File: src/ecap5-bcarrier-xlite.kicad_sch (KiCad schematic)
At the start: 27 parts, among them J3 VIN9_15, J4 GND, J5 USB_C_Receptacle_USB2.0_14P, SW1 RESET_SOM1, SW2 RESET_SOM2, SW3 USER1, SW4 USER2, U2 AP7375-33SA-7

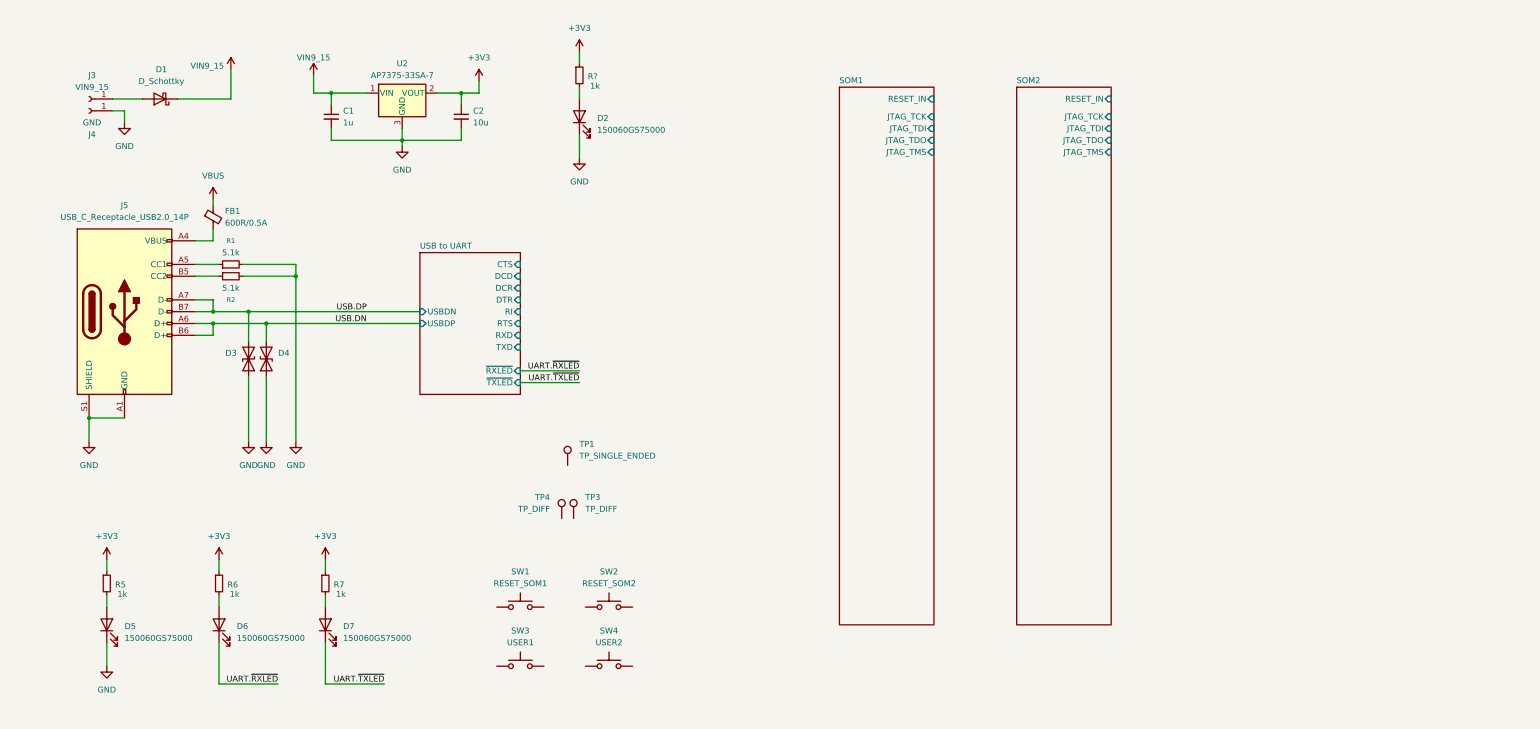
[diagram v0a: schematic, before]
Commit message: Add LED driver
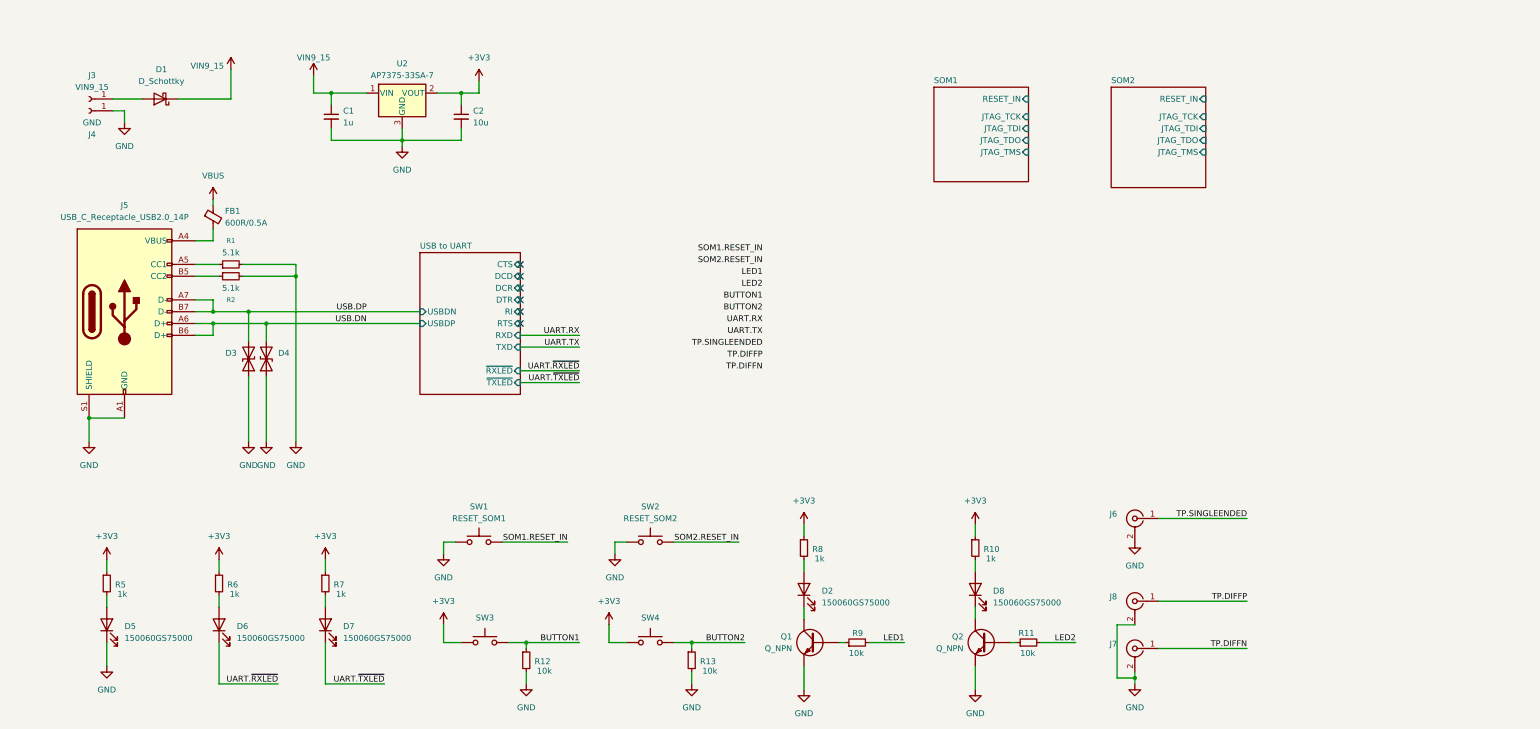
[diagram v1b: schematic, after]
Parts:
- removed R?: 1k, Resistor_SMD:R_0402_1005Metric, symbol Device:R_Small
- removed TP1: TP_SINGLE_ENDED, symbol Connector:TestPoint
- removed TP3, TP4: TP_DIFF, symbol Connector:TestPoint
- added D8: 150060GS75000, LED_SMD:LED_0603_1608Metric, symbol Device:LED
- added J6, J7, J8: Conn_Coaxial, symbol Connector:Conn_Coaxial
- added Q1, Q2: Q_NPN, symbol Device:Q_NPN
- added R10, R8: 1k, Resistor_SMD:R_0402_1005Metric, symbol Device:R_Small
- added R11, R12, R13, R9: 10k, Resistor_SMD:R_0402_1005Metric, symbol Device:R_Small
- SW4: value USER2 -> USER1
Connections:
- net +3V3: now also SW3.1, SW4.1, R10.1, R8.1
- net GND: now also SW1.1, SW2.1, J6.2 (Ext), J7.2 (Ext), J8.2 (Ext), Q1.E, Q2.E, R12.2, R13.2; no longer D2.1 (K)
- net SOM2.RESET_IN: now reaches SW2.2
- net SOM1.RESET_IN: now reaches SW1.2
- net at D2.2 (A): now also R8.2
- net BUTTON2: now reaches SW4.2
- net BUTTON2: now also R13.1
- net BUTTON1: now reaches SW3.2
- net BUTTON1: now also R12.1
- new net: Q2.B, R11.1
- new net: D8.1 (K), Q2.C
- new net: D2.1 (K), Q1.C
- new net: Q1.B, R9.1
- new net: D8.2 (A), R10.2
- new net LED1: R9.2
- new net LED2: R11.2
- new net TP.DIFFN: J7.1 (In)
- new net TP.DIFFP: J8.1 (In)
- new net TP.SINGLEENDED: J6.1 (In)
- no-connect marks 0 -> 6
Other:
- moved on the sheet: SW1, SW2, SW3

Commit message: Add component footprints
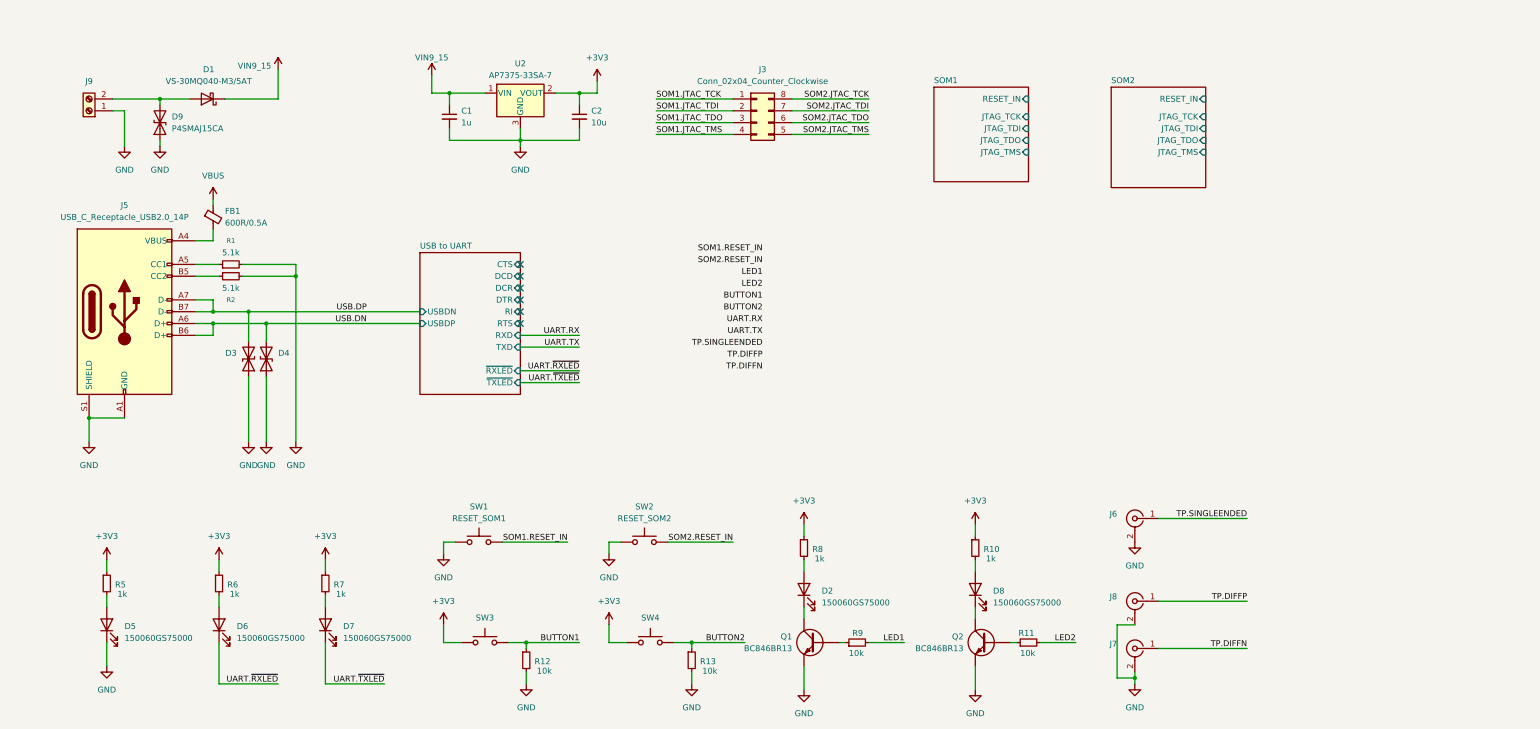
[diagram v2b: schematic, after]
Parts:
- removed J3: VIN9_15, symbol Connector:Conn_01x01_Socket
- removed J4: GND, symbol Connector:Conn_01x01_Socket
- added D9: P4SMAJ15CA, Diode_SMD:D_SMA, symbol Device:D_TVS
- added J3: Conn_02x04_Counter_Clockwise, Connector_PinSocket_2.54mm:PinSocket_2x04_P2.54mm_Vertical, symbol Connector_Generic:Conn_02x04_Counter_Clockwise
- added J9: 1935161, TerminalBlock_Phoenix:TerminalBlock_Phoenix_PT-1,5-2-5.0-H_1x02_P5.00mm_Horizontal, symbol Connector:Screw_Terminal_01x02
- C1, C2: footprint (none) -> Capacitor_SMD:C_0603_1608Metric
- D1: value D_Schottky -> VS-30MQ040-M3/5AT; footprint (none) -> Diode_SMD:D_SMA
- D3, D4: value D_TVS -> ESD321DYAR; footprint (none) -> Diode_SMD:D_SOD-523
- FB1: footprint (none) -> Inductor_SMD:L_0603_1608Metric; Part (none) -> MMZ1608Y601BTA00
- J5: footprint (none) -> Connector_USB:USB_C_Receptacle_GCT_USB4105-xx-A_16P_TopMnt_Horizontal; Part (none) -> USB4105-GF-A
- J6, J7, J8: footprint (none) -> Connector_Coaxial:SMA_Amphenol_132134-10_Vertical
- Q1, Q2: value Q_NPN -> BC846BR13; footprint (none) -> Package_TO_SOT_SMD:SOT-23-3
- R1, R2: footprint (none) -> Resistor_SMD:R_0603_1608Metric
- R10, R11, R12, R13, R5, R6, R7, R8, R9: footprint Resistor_SMD:R_0402_1005Metric -> Resistor_SMD:R_0603_1608Metric
- SW1, SW2, SW3, SW4: footprint (none) -> Button_Switch_SMD:SW_Push_1P1T_NO_CK_PTS125Sx73SMTR; Part (none) -> PTS125SM73SMTR21M LFS
- U2: footprint (none) -> Package_TO_SOT_SMD:SOT-23-3
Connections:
- net GND: now also D9.1 (A1), J9.1 (Pin_1)
- net at D1.2 (A): now also D9.2 (A2), J9.2 (Pin_2)
- new net SOM1.JTAC_TCK: J3.1 (Pin_1)
- new net SOM1.JTAC_TDI: J3.2 (Pin_2)
- new net SOM1.JTAC_TDO: J3.3 (Pin_3)
- new net SOM1.JTAC_TMS: J3.4 (Pin_4)
- new net SOM2.JTAC_TCK: J3.8 (Pin_8)
- new net SOM2.JTAC_TDI: J3.7 (Pin_7)
- new net SOM2.JTAC_TDO: J3.6 (Pin_6)
- new net SOM2.JTAC_TMS: J3.5 (Pin_5)
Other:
- moved on the sheet: C1, C2, D1, SW2, U2

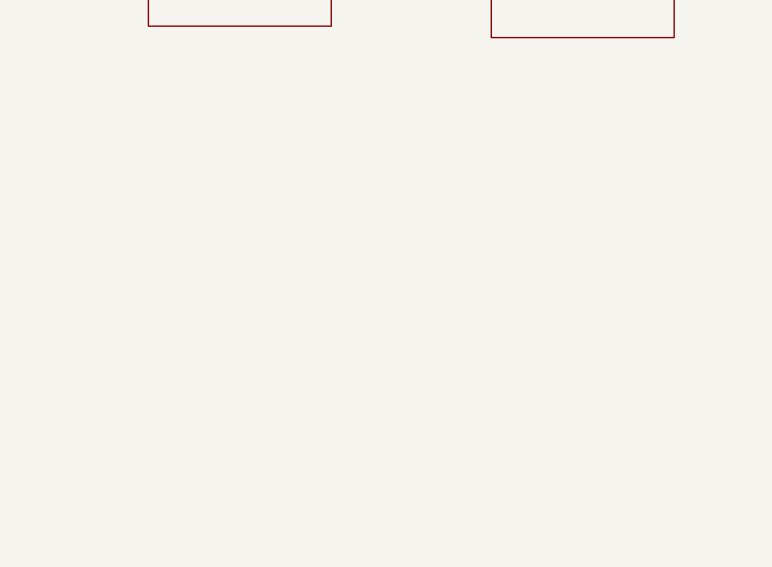
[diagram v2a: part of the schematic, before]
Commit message: Add power planes
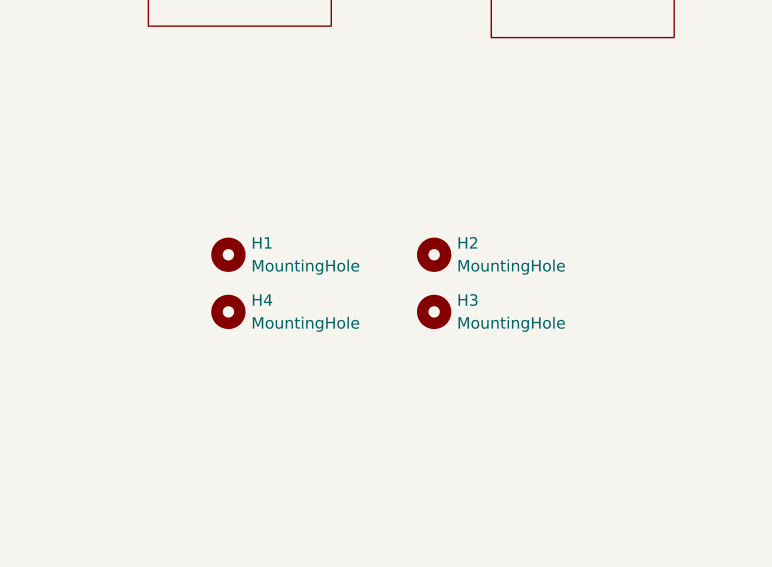
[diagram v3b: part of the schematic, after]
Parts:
- added H1, H2, H3, H4: MountingHole, MountingHole:MountingHole_2.2mm_M2, symbol Mechanical:MountingHole
- J3: footprint Connector_PinSocket_2.54mm:PinSocket_2x04_P2.54mm_Vertical -> Connector_PinHeader_2.54mm:PinHeader_2x04_P2.54mm_Vertical

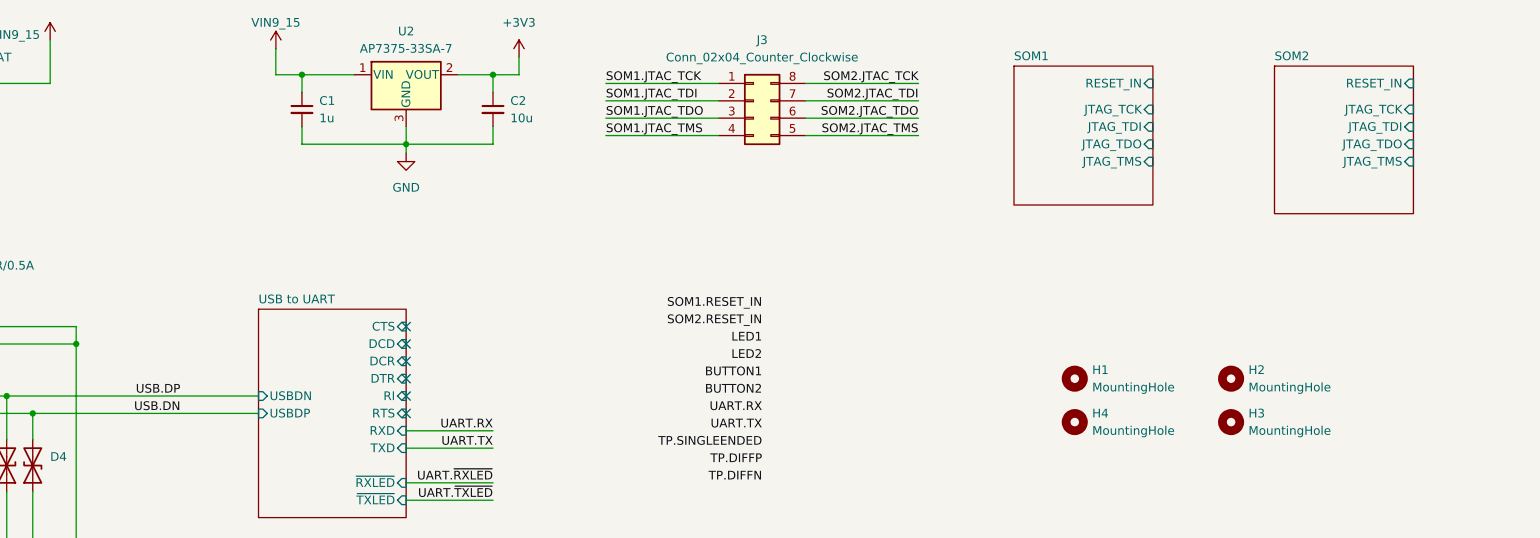
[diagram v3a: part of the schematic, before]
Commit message: Start routing the usb interface
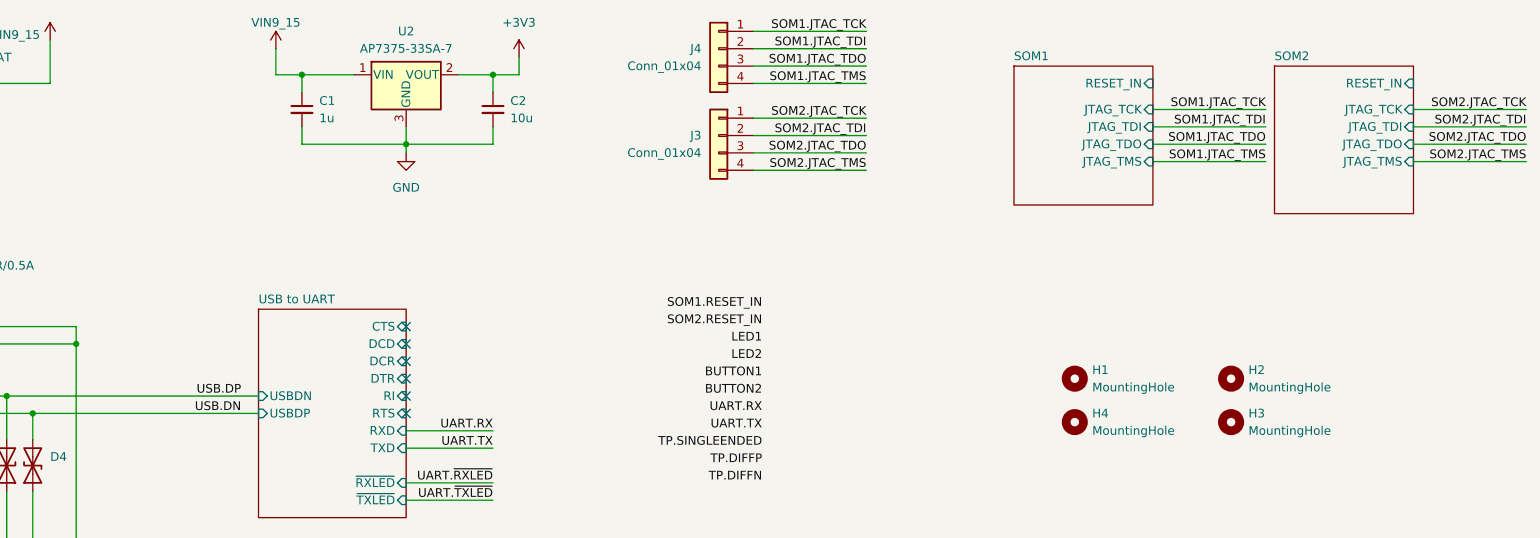
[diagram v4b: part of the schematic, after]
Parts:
- removed J3: Conn_02x04_Counter_Clockwise, Connector_PinHeader_2.54mm:PinHeader_2x04_P2.54mm_Vertical, symbol Connector_Generic:Conn_02x04_Counter_Clockwise
- added J3, J4: Conn_01x04, Connector_PinHeader_2.54mm:PinHeader_1x04_P2.54mm_Vertical, symbol Connector_Generic:Conn_01x04
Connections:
- net SOM1.JTAC_TCK: now also J4.1 (Pin_1)
- net SOM1.JTAC_TDI: now also J4.2 (Pin_2)
- net SOM1.JTAC_TDO: now also J4.3 (Pin_3)
- net SOM1.JTAC_TMS: now also J4.4 (Pin_4)
- net SOM2.JTAC_TCK: now also J3.1 (Pin_1)
- net SOM2.JTAC_TDI: now also J3.2 (Pin_2)
- net SOM2.JTAC_TDO: now also J3.3 (Pin_3)
- net SOM2.JTAC_TMS: now also J3.4 (Pin_4)
